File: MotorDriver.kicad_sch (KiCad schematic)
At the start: 0 parts

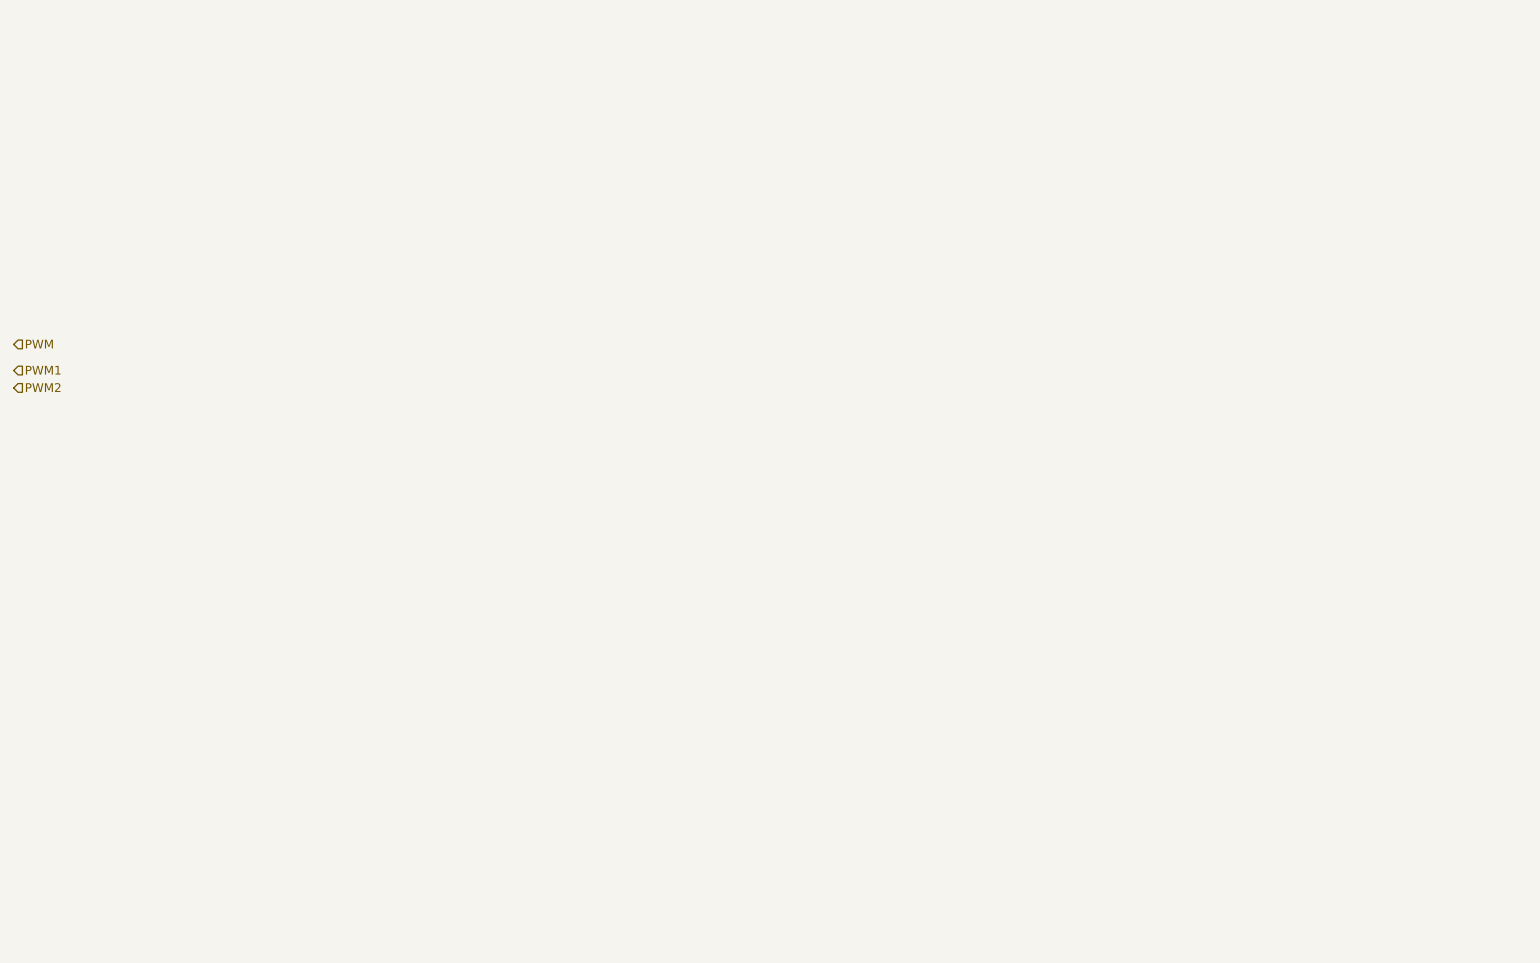
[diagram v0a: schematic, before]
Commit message: seprate motors
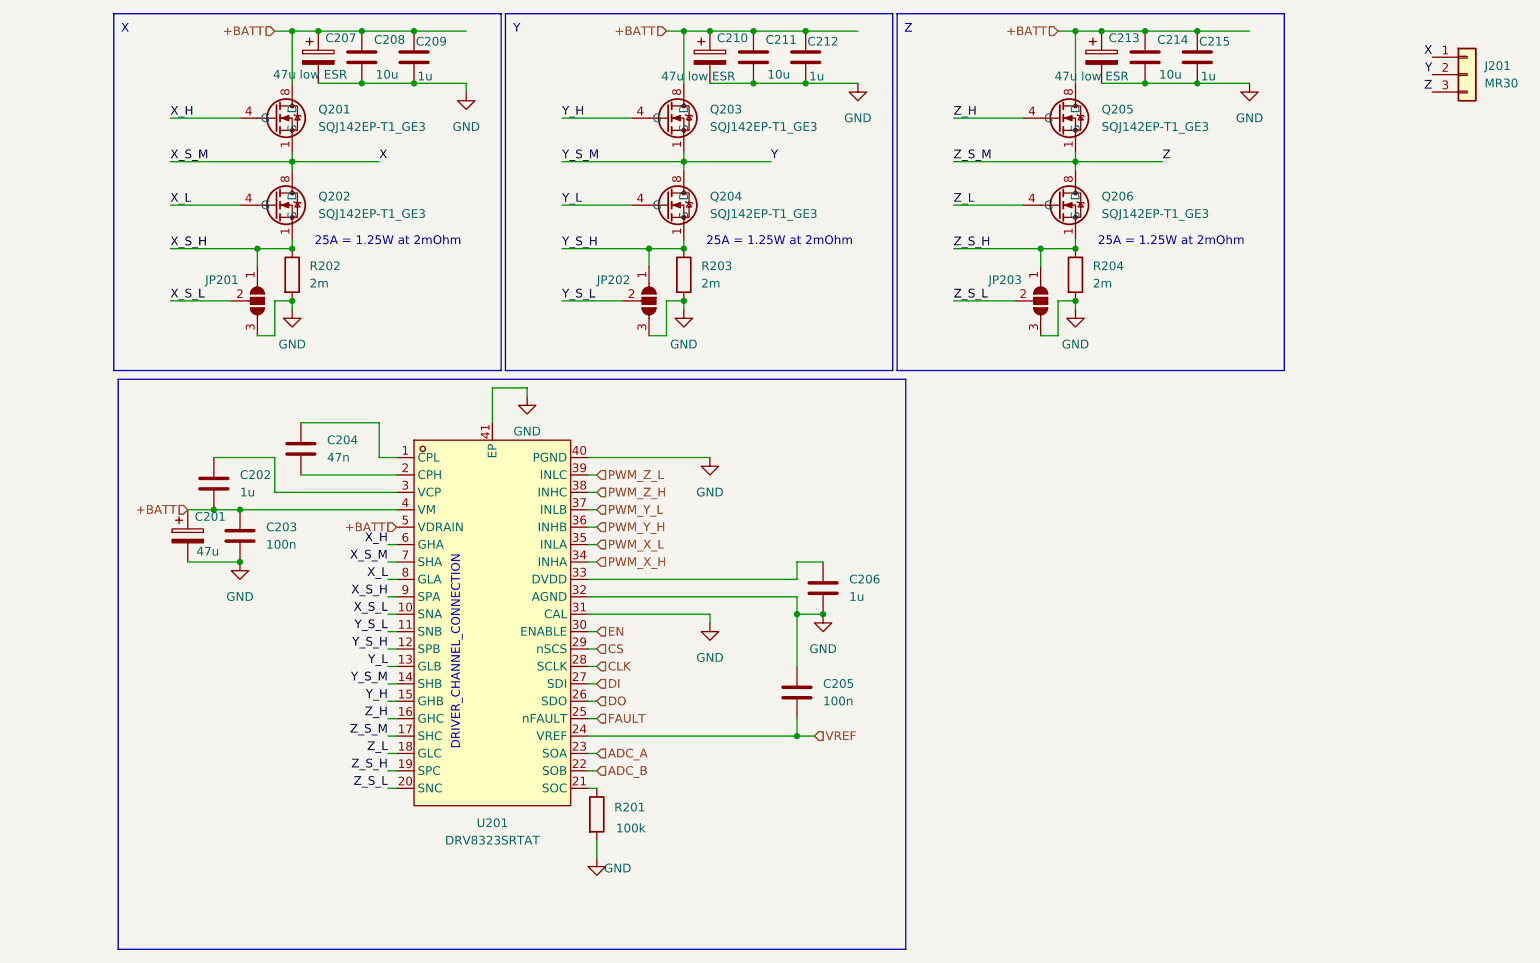
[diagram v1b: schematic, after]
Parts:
- added C201: 47u, Capacitor_THT:CP_Radial_D6.3mm_P2.50mm, symbol Device:C_Polarized
- added C202, C206, C209, C212, C215: 1u, COMPONENTS:1206_Resistor, symbol Device:C
- added C203, C205: 100n, COMPONENTS:1206_Resistor, symbol Device:C
- added C204: 47n, COMPONENTS:1206_Resistor, symbol Device:C
- added C207, C210, C213: 47u low ESR, Capacitor_THT:CP_Radial_D6.3mm_P2.50mm, symbol Device:C_Polarized
- added C208, C211, C214: 10u, COMPONENTS:1206_Resistor, symbol Device:C
- added J201: MR30, Connector_AMASS:AMASS_MR30PW-FB_1x03_P3.50mm_Horizontal, symbol Connector_Generic:Conn_01x03
- added JP201, JP202, JP203: SolderJumper_3_Open, Jumper:SolderJumper-3_P1.3mm_Open_RoundedPad1.0x1.5mm_NumberLabels, symbol Jumper:SolderJumper_3_Open
- added Q201, Q202, Q203, Q204, Q205, Q206: SQJ142EP-T1_GE3, JLCPCB_Transistors_Thyristors:POWERPAK-SO-8_L5.9-W4.9-P1.27-BL, symbol JLCPCB_Transistors_Thyristors:SQJ142EP-T1_GE3
- added R201: 100k, COMPONENTS:1206_Resistor, symbol Device:R
- added R202, R203, R204: 2m, COMPONENTS:1206_Resistor, symbol Device:R
- added U201: DRV8323SRTAT, JLCPCB_Power_Supply_Chip:WQFN-40_L6.0-W6.0-P0.50-TL-EP4.5, symbol JLCPCB_Power_Supply_Chip:DRV8323SRTAT
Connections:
- new net: C202.1, U201.3 (VCP)
- new net: C204.1, U201.1 (CPL)
- new net: C204.2, U201.2 (CPH)
- new net: R201.1, U201.21 (SOC)
- new net: C206.1, U201.33 (DVDD)
- new net +BATT: C201.1, C202.2, C203.1, C207.1, C208.1, C209.1, C210.1, C211.1, C212.1, C213.1, C214.1, C215.1, Q201.8 (D), Q203.8 (D), Q205.8 (D), U201.4 (VM), U201.5 (VDRAIN)
- new net ADC_A: U201.23 (SOA)
- new net ADC_B: U201.22 (SOB)
- new net CLK: U201.28 (SCLK)
- new net CS: U201.29 (nSCS)
- new net DI: U201.27 (SDI)
- new net DO: U201.26 (SDO)
- new net EN: U201.30 (ENABLE)
- new net FAULT: U201.25 (nFAULT)
- new net GND: C201.2, C203.2, C205.1, C206.2, C207.2, C208.2, C209.2, C210.2, C211.2, C212.2, C213.2, C214.2, C215.2, JP201.3 (B), JP202.3 (B), JP203.3 (B), R201.2, R202.2, R203.2, R204.2, U201.31 (CAL), U201.32 (AGND), U201.40 (PGND), U201.41 (EP)
- new net PWM_X_H: U201.34 (INHA)
- new net PWM_X_L: U201.35 (INLA)
- new net PWM_Y_H: U201.36 (INHB)
- new net PWM_Y_L: U201.37 (INLB)
- new net PWM_Z_H: U201.38 (INHC)
- new net PWM_Z_L: U201.39 (INLC)
- new net VREF: C205.2, U201.24 (VREF)
- new net X: J201.1 (Pin_1), Q201.1 (S), Q202.8 (D), U201.7 (SHA)
- new net X_H: Q201.4 (G), U201.6 (GHA)
- new net X_L: Q202.4 (G), U201.8 (GLA)
- new net X_S_H: JP201.1 (A), Q202.1 (S), R202.1, U201.9 (SPA)
- new net X_S_L: JP201.2 (C), U201.10 (SNA)
- new net Y: J201.2 (Pin_2), Q203.1 (S), Q204.8 (D), U201.14 (SHB)
- new net Y_H: Q203.4 (G), U201.15 (GHB)
- new net Y_L: Q204.4 (G), U201.13 (GLB)
- new net Y_S_H: JP202.1 (A), Q204.1 (S), R203.1, U201.12 (SPB)
- new net Y_S_L: JP202.2 (C), U201.11 (SNB)
- new net Z: J201.3 (Pin_3), Q205.1 (S), Q206.8 (D), U201.17 (SHC)
- new net Z_H: Q205.4 (G), U201.16 (GHC)
- new net Z_L: Q206.4 (G), U201.18 (GLC)
- new net Z_S_H: JP203.1 (A), Q206.1 (S), R204.1, U201.19 (SPC)
- new net Z_S_L: JP203.2 (C), U201.20 (SNC)
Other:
- note added: "25A = 1.25W at 2mOhm"
- note added: "DRIVER_CHANNEL_CONNECTION"
- note added: "X"
- note added: "Y"
- note added: "Z"
